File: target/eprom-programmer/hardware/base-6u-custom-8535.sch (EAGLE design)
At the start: 20 parts, among them IC1 MEGA8535-P

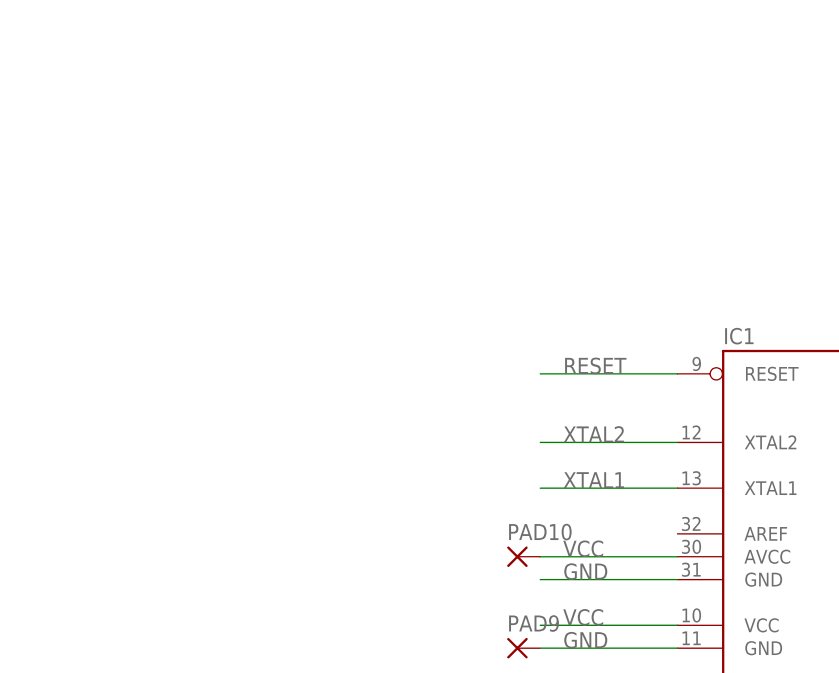
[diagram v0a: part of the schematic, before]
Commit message: eprom-programmer: hardware
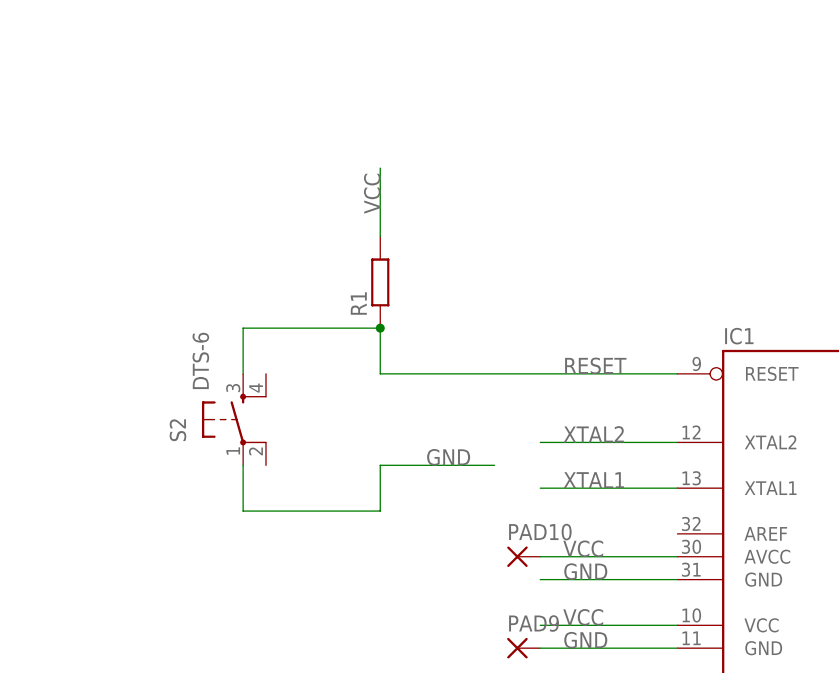
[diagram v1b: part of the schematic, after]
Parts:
- added R1: (no value), rcl:R-EU_0204/2V
- added S2: DTS-6, switch-tact:DTS-6
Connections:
- net GND: now also S2.1
- net RESET: now also R1.1, S2.3
- net VCC: now also R1.2
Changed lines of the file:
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@@
 <part name="PAD2" library="wirepad" deviceset="1,6/0,8" device=""/>
 <part name="PAD3" library="wirepad" deviceset="1,6/0,8" device=""/>
+<part name="S2" library="switch-tact" deviceset="DTS-6" device=""/>
+<part name="R1" library="rcl" deviceset="R-EU_" device="0204/2V"/>
 </parts>
 <sheets>
@@
 <instance part="PAD2" gate="P" x="185.42" y="-127" rot="R180"/>
 <instance part="PAD3" gate="P" x="53.34" y="-93.98" rot="R180"/>
+<instance part="S2" gate="G$1" x="78.74" y="-48.26"/>
+<instance part="R1" gate="G$1" x="93.98" y="-33.02" rot="R90"/>
 </instances>
 <busses>
@@
 <label x="208.28" y="-134.62" size="1.778" layer="95"/>
 </segment>
+<segment>
+<wire x1="93.98" y1="-53.34" x2="106.68" y2="-53.34" width="0.1524" layer="91"/>
+<label x="99.06" y="-53.34" size="1.778" layer="95"/>
+<pinref part="S2" gate="G$1" pin="1"/>
+<wire x1="78.74" y1="-53.34" x2="78.74" y2="-58.42" width="0.1524" layer="91"/>
+<wire x1="78.74" y1="-58.42" x2="93.98" y2="-58.42" width="0.1524" layer="91"/>
+<wire x1="93.98" y1="-58.42" x2="93.98" y2="-53.34" width="0.1524" layer="91"/>
+</segment>
 </net>
 <net name="VCC" class="0">
@@
 <wire x1="236.22" y1="-134.62" x2="251.46" y2="-134.62" width="0.1524" layer="91"/>
 <label x="238.76" y="-134.62" size="1.778" layer="95"/>
+</segment>
+<segment>
+<pinref part="R1" gate="G$1" pin="2"/>
+<wire x1="93.98" y1="-27.94" x2="93.98" y2="-20.32" width="0.1524" layer="91"/>
+<label x="93.98" y="-25.4" size="1.778" layer="95" rot="R90"/>
 </segment>
 </net>
@@
 <segment>
 <pinref part="IC1" gate="G$1" pin="RESET"/>
-<wire x1="127" y1="-43.18" x2="111.76" y2="-43.18" width="0.1524" layer="91"/>
 <label x="114.3" y="-43.18" size="1.778" layer="95"/>
-</segment>
-<segment>
+<wire x1="93.98" y1="-43.18" x2="127" y2="-43.18" width="0.1524" layer="91"/>
+<pinref part="S2" gate="G$1" pin="3"/>
+<wire x1="78.74" y1="-43.18" x2="78.74" y2="-38.1" width="0.1524" layer="91"/>
+<wire x1="78.74" y1="-38.1" x2="93.98" y2="-38.1" width="0.1524" layer="91"/>
+<wire x1="93.98" y1="-38.1" x2="93.98" y2="-43.18" width="0.1524" layer="91"/>
+<pinref part="R1" gate="G$1" pin="1"/>
+<junction x="93.98" y="-38.1"/>
+</segment>
+<segment>
